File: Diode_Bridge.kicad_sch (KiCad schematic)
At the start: 0 parts

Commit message: diode bridge
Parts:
- added C3, C4: C, symbol Device:C
- added D1, D2, D3, D4: D, symbol Device:D
- added L1: L, Relay_THT:Relay_DPDT_Finder_30.22, symbol Device:L
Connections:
- net GND: now also C3.2, C4.2, D2.2 (A), D3.2 (A)
- new net: C4.1, D1.1 (K), D4.1 (K), L1.1
- new net: D1.2 (A), D2.1 (K)
- new net: C3.1, L1.2
- new net: D3.1 (K), D4.2 (A)

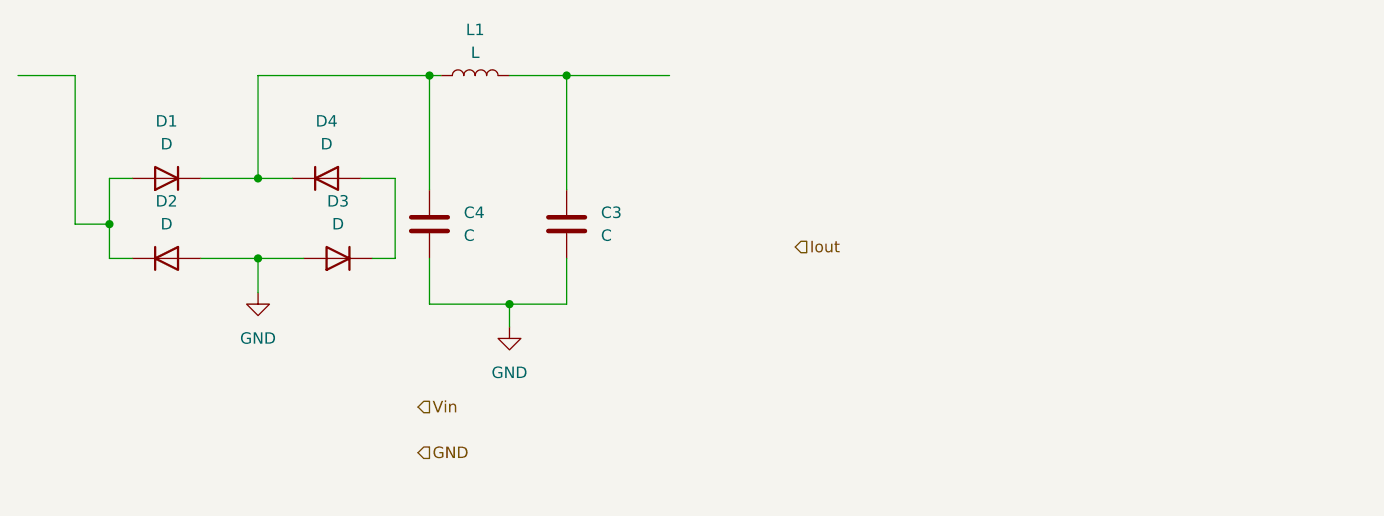
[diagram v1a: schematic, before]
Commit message: Fixed Diode bridge
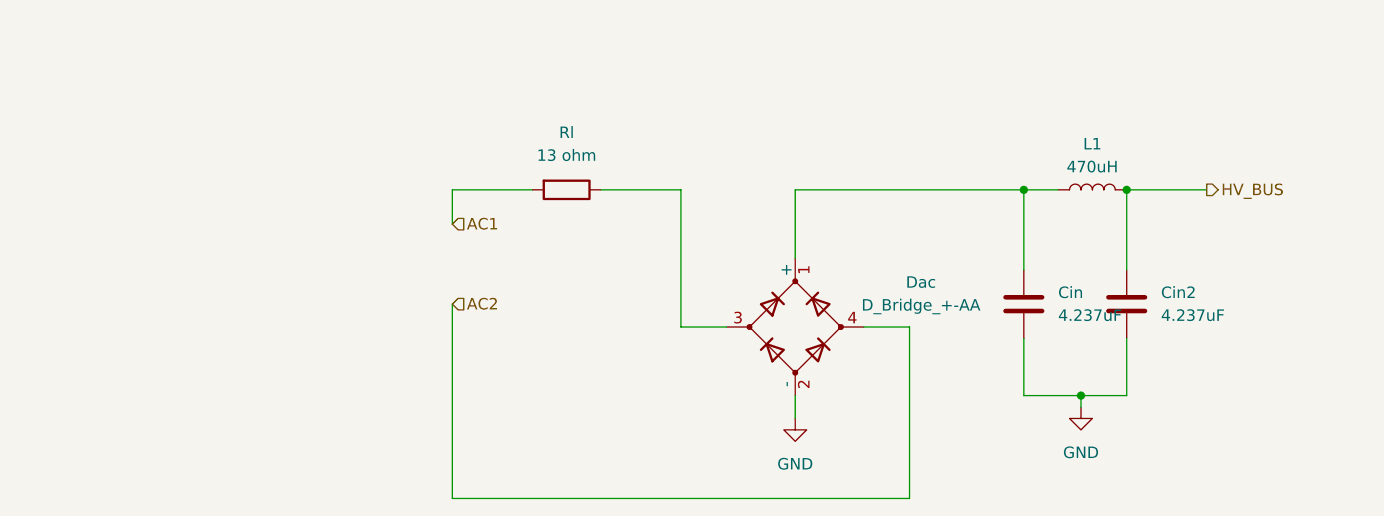
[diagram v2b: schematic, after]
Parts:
- removed C3, C4: C, symbol Device:C
- removed D1, D2, D3, D4: D, symbol Device:D
- added Cin, Cin2: 4.237uF, symbol Device:C
- added Dac: D_Bridge_+-AA, symbol Device:D_Bridge_+-AA
- added Rl: 13 ohm, symbol Device:R
- L1: value L -> 470uH; footprint Relay_THT:Relay_DPDT_Finder_30.22 -> (none)
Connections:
- net GND: now also Cin.2, Cin2.2, Dac.2 (-)
- net at L1.1: now also Cin.1, Dac.1 (+)
- net HV_BUS: now reaches L1.2
- net HV_BUS: now also Cin2.1
- new net: Dac.3, Rl.1
- new net AC1: Rl.2
- new net AC2: Dac.4

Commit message: Diode bridge
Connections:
- net AC2 is gone; now on net GND: Dac.4
- net AC1 renamed Vin
- net HV_BUS renamed Iout
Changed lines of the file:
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@@
 		)
 	)
-	(hierarchical_label "HV_BUS"
+	(hierarchical_label "Iout"
 		(shape output)
 		(at 172.72 67.31 0)
@@
 		)
 	)
-	(hierarchical_label "AC1"
+	(hierarchical_label "Vin"
 		(shape input)
 		(at 88.9 71.12 0)
@@
 		)
 	)
-	(hierarchical_label "AC2"
+	(hierarchical_label "GND"
 		(shape input)
 		(at 88.9 80.01 0)

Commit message: footprints
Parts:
- removed Dac: D_Bridge_+-AA, symbol Device:D_Bridge_+-AA
- added Dac (x3): D, Diode_THT:D_DO-15_P15.24mm_Horizontal, symbol Device:D
- added Dac: D, Diode_THT:D_DO-201AD_P15.24mm_Horizontal, symbol Device:D
- Cin, Cin2: footprint (none) -> Capacitor_THT:C_Disc_D10.0mm_W2.5mm_P5.00mm
- L1: footprint (none) -> Inductor_THT:L_Axial_L6.6mm_D2.7mm_P2.54mm_Vertical_Vishay_IM-2
- Rl: footprint (none) -> Resistor_THT:R_Axial_DIN0207_L6.3mm_D2.5mm_P7.62mm_Horizontal
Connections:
- net GND: now also Dac.1 (K), Dac.2 (A), Dac.2 (A), Dac.2 (A)
- net at Cin.1, L1.1: now also Dac.1 (K), Dac.1 (K)
- net at Rl.1: now also Dac.1 (K), Dac.2 (A)

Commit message: Added sheet pins
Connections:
- net GND: no longer Dac.1 (K), Dac.2 (A)
- net Iout renamed Rectifier_Out
- net Vin renamed Wall_Voltage_In
- new net Wall_Ground: Dac.1 (K), Dac.2 (A)
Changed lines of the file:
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@@
 	(wire
 		(pts
-			(xy 88.9 67.31) (xy 88.9 71.12)
+			(xy 83.82 67.31) (xy 83.82 71.12)
 		)
 		(stroke
@@
 	(wire
 		(pts
-			(xy 97.79 67.31) (xy 88.9 67.31)
-		)
-		(stroke
-			(width 0)
-			(type default)
-		)
-	)
-	(wire
-		(pts
-			(xy 88.9 80.01) (xy 88.9 101.6)
+			(xy 97.79 67.31) (xy 83.82 67.31)
+		)
+		(stroke
+			(width 0)
+			(type default)
+		)
+	)
+	(wire
+		(pts
+			(xy 88.9 93.98) (xy 88.9 101.6)
 		)
 		(stroke
@@
 		)
 	)
-	(hierarchical_label "Iout"
+	(hierarchical_label "Rectifier_Out"
 		(shape output)
 		(at 172.72 67.31 0)
@@
 		)
 	)
-	(hierarchical_label "Vin"
+	(hierarchical_label "Wall_Voltage_In"
 		(shape input)
-		(at 88.9 71.12 0)
+		(at 83.82 71.12 270)
 		(effects
 			(font
 				(size 1.27 1.27)
 			)
-			(justify left)
-		)
-	)
-	(hierarchical_label "GND"
+			(justify right)
+		)
+	)
+	(hierarchical_label "Wall_Ground"
 		(shape input)
-		(at 88.9 80.01 0)
+		(at 88.9 93.98 90)
 		(effects
 			(font

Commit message: FixedMostIssues
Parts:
- renumbered Cin to Cin1, Dac to Dac1, Dac to Dac2, Dac to Dac3, Dac to Dac4, L1 to L2, Rl to Rl1
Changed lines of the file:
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@@
 		(dnp no)
 		(fields_autoplaced yes)
-		(property "Reference" "L1"
+		(property "Reference" "L2"
 			(at 160.02 62.23 90)
 			(show_name no)
@@
 			(project "Solar_Battery"
 				(path "/6805959e-39bb-4644-b93e-3970e29fedc0/a320594e-eb17-43a9-8193-2f75b3718179/66c5df4f-46ad-4d4f-997c-052ec03a6539"
-					(reference "L1")
+					(reference "L2")
 					(unit 1)
 				)
@@
 		(dnp no)
 		(fields_autoplaced yes)
-		(property "Reference" "Rl"
+		(property "Reference" "Rl1"
 			(at 101.6 60.96 90)
 			(show_name no)
@@
 			(project "Solar_Battery"
 				(path "/6805959e-39bb-4644-b93e-3970e29fedc0/a320594e-eb17-43a9-8193-2f75b3718179/66c5df4f-46ad-4d4f-997c-052ec03a6539"
-					(reference "Rl")
+					(reference "Rl1")
 					(unit 1)
 				)
@@
 		(dnp no)
 		(fields_autoplaced yes)
-		(property "Reference" "#PWR02"
+		(property "Reference" "#PWR014"
 			(at 158.75 97.79 0)
 			(hide yes)
@@
 			(project "Solar_Battery"
 				(path "/6805959e-39bb-4644-b93e-3970e29fedc0/a320594e-eb17-43a9-8193-2f75b3718179/66c5df4f-46ad-4d4f-997c-052ec03a6539"
-					(reference "#PWR02")
+					(reference "#PWR014")
 					(unit 1)
 				)
@@
 		(dnp no)
 		(fields_autoplaced yes)
-		(property "Reference" "Dac"
+		(property "Reference" "Dac2"
 			(at 123.19 78.74 0)
 			(show_name no)
@@
 			(project "Solar_Battery"
 				(path "/6805959e-39bb-4644-b93e-3970e29fedc0/a320594e-eb17-43a9-8193-2f75b3718179/66c5df4f-46ad-4d4f-997c-052ec03a6539"
-					(reference "Dac")
+					(reference "Dac2")
 					(unit 1)
 				)
@@
 		(dnp no)
 		(fields_autoplaced yes)
-		(property "Reference" "Dac"
+		(property "Reference" "Dac3"
 			(at 133.35 68.58 0)
 			(show_name no)
@@
 			(project "Solar_Battery"
 				(path "/6805959e-39bb-4644-b93e-3970e29fedc0/a320594e-eb17-43a9-8193-2f75b3718179/66c5df4f-46ad-4d4f-997c-052ec03a6539"
-					(reference "Dac")
+					(reference "Dac3")
 					(unit 1)
 				)
@@
 		(dnp no)
 		(fields_autoplaced yes)
-		(property "Reference" "Dac"
+		(property "Reference" "Dac4"
 			(at 133.35 78.74 0)
 			(show_name no)
@@
 			(project "Solar_Battery"
 				(path "/6805959e-39bb-4644-b93e-3970e29fedc0/a320594e-eb17-43a9-8193-2f75b3718179/66c5df4f-46ad-4d4f-997c-052ec03a6539"
-					(reference "Dac")
+					(reference "Dac4")
 					(unit 1)
 				)
@@
 		(dnp no)
 		(fields_autoplaced yes)
-		(property "Reference" "#PWR03"
+		(property "Reference" "#PWR013"
 			(at 127 99.06 0)
 			(hide yes)
@@
 			(project "Solar_Battery"
 				(path "/6805959e-39bb-4644-b93e-3970e29fedc0/a320594e-eb17-43a9-8193-2f75b3718179/66c5df4f-46ad-4d4f-997c-052ec03a6539"
-					(reference "#PWR03")
+					(reference "#PWR013")
 					(unit 1)
 				)
@@
 		(dnp no)
 		(fields_autoplaced yes)
-		(property "Reference" "Dac"
+		(property "Reference" "Dac1"
 			(at 120.65 68.58 0)
 			(show_name no)
@@
 			(project "Solar_Battery"
 				(path "/6805959e-39bb-4644-b93e-3970e29fedc0/a320594e-eb17-43a9-8193-2f75b3718179/66c5df4f-46ad-4d4f-997c-052ec03a6539"
-					(reference "Dac")
+					(reference "Dac1")
 					(unit 1)
 				)
@@
 		(dnp no)
 		(fields_autoplaced yes)
-		(property "Reference" "Cin"
+		(property "Reference" "Cin1"
 			(at 156.21 78.7399 0)
 			(show_name no)
@@
 			(project "Solar_Battery"
 				(path "/6805959e-39bb-4644-b93e-3970e29fedc0/a320594e-eb17-43a9-8193-2f75b3718179/66c5df4f-46ad-4d4f-997c-052ec03a6539"
-					(reference "Cin")
-					(unit 1)
-				)
+					(reference "Cin1")
+					(unit 1)
+				)
